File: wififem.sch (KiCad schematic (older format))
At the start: 46 parts, among them J1 Conn_Coaxial, J2 Conn_Coaxial, J3 Conn_Coaxial, J4 Conn_01x05, U1 MCP6566, U2 74HCT04, U3 SE2611T, U4 AP1117-15

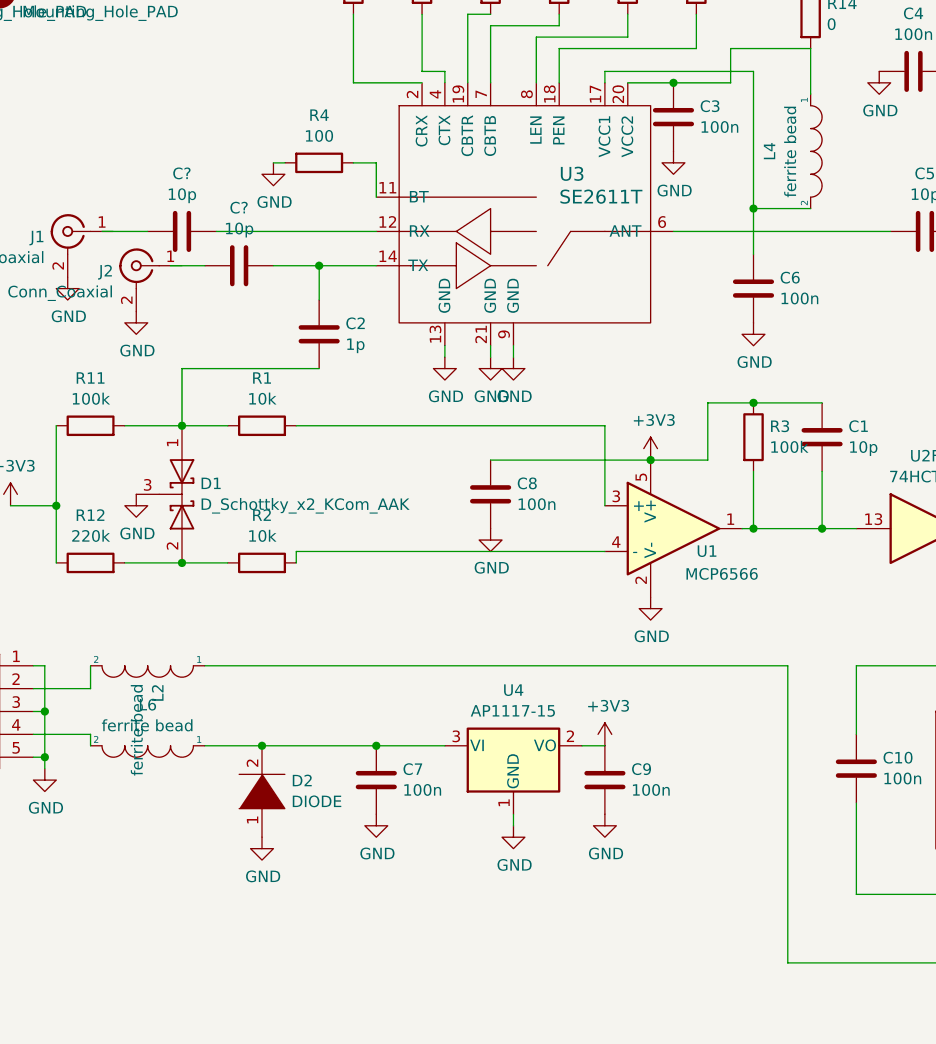
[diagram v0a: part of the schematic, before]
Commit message: Add 2.2u decoupling, some layout changes
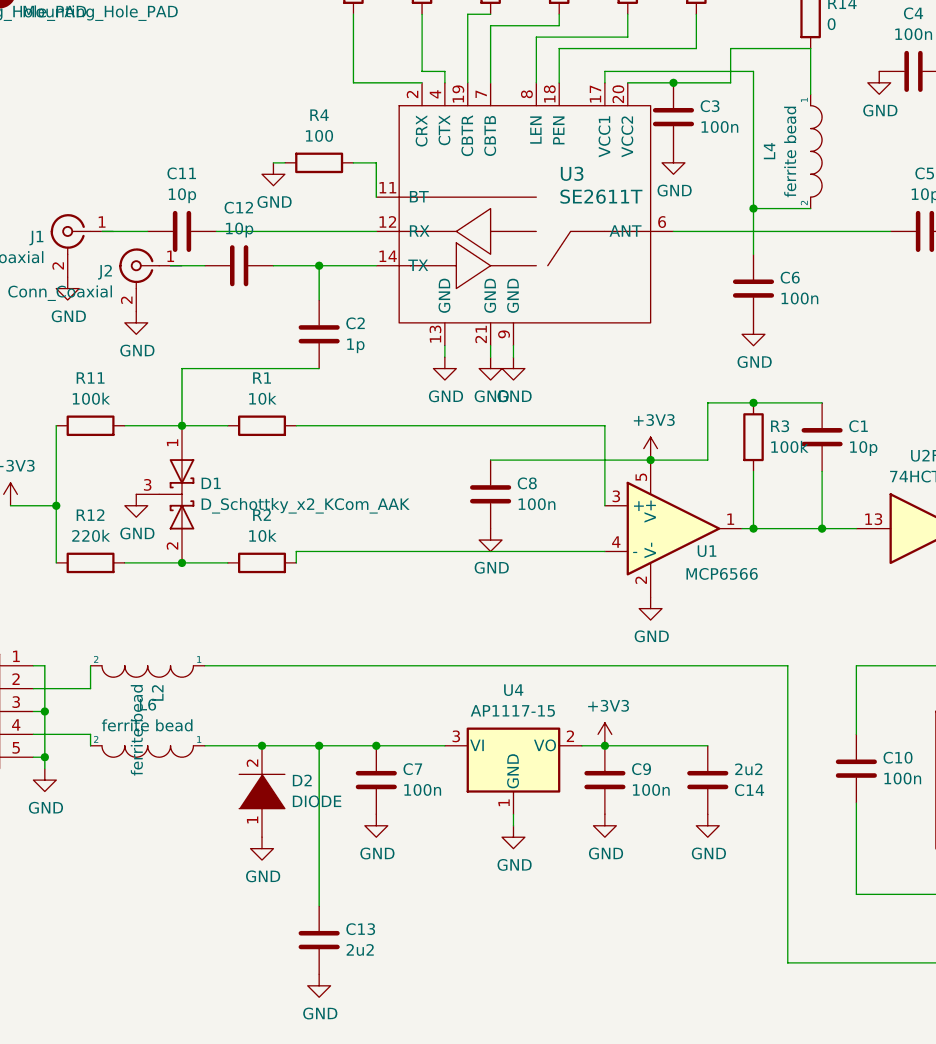
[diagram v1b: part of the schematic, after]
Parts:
- added C13, C14: 2u2, Capacitors_SMD:C_0603_HandSoldering, symbol device:C
- gave numbers to parts that had none: 2
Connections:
- net +3V3: now also C14.1
- net GND: now also C13.1, C14.2
- net at C7.2, D2.2 (A), L6.1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: now also C13.2
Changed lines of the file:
@@
 Connection ~ 3600 3850
 Wire Wire Line
-	6000 4900 5900 4900
+	5900 4900 6450 4900
 Wire Wire Line
 	5600 5250 5600 5200
@@
 Connection ~ 6650 2550
 $Comp
-L device:C C?
+L device:C C11
 U 1 1 5A1C7E8A
 P 4150 2650
-F 0 "C?" V 3898 2650 50  0000 C CNN
+F 0 "C11" V 3898 2650 50  0000 C CNN
 F 1 "10p" V 3989 2650 50  0000 C CNN
 F 2 "Capacitors_SMD:C_0805_HandSoldering" H 4188 2500 50  0001 C CNN
@@
 	4150 3250 4150 3500
 $Comp
-L device:C C?
+L device:C C12
 U 1 1 5A1D3989
 P 4400 2800
-F 0 "C?" V 4148 2800 50  0000 C CNN
+F 0 "C12" V 4148 2800 50  0000 C CNN
 F 1 "10p" V 4239 2800 50  0000 C CNN
 F 2 "Capacitors_SMD:C_0805_HandSoldering" H 4438 2650 50  0001 C CNN
@@
 Wire Wire Line
 	4300 2650 5000 2650
+$Comp
+L device:C C13
+U 1 1 5A1F21AD
+P 4750 5750
+F 0 "C13" H 4635 5704 50  0000 R CNN
+F 1 "2u2" H 4635 5795 50  0000 R CNN
+F 2 "Capacitors_SMD:C_0603_HandSoldering" H 4788 5600 50  0001 C CNN
+F 3 "" H 4750 5750 50  0001 C CNN
+	1    4750 5750
+	-1   0    0    1
+$EndComp
+Wire Wire Line
+	4750 5600 4750 4900
+Connection ~ 4750 4900
+$Comp
+L power:GND #PWR017
+U 1 1 5A1F72C9
+P 4750 5900
+F 0 "#PWR017" H 4750 5650 50  0001 C CNN
+F 1 "GND" H 4755 5727 50  0000 C CNN
+F 2 "" H 4750 5900 50  0001 C CNN
+F 3 "" H 4750 5900 50  0001 C CNN
+	1    4750 5900
+	1    0    0    -1
+$EndComp
+$Comp
+L device:C C14
+U 1 1 5A1F733E
+P 6450 5050
+F 0 "C14" H 6335 5004 50  0000 R CNN
+F 1 "2u2" H 6335 5095 50  0000 R CNN
+F 2 "Capacitors_SMD:C_0603_HandSoldering" H 6488 4900 50  0001 C CNN
+F 3 "" H 6450 5050 50  0001 C CNN
+	1    6450 5050
+	-1   0    0    -1
+$EndComp
+Connection ~ 6000 4900
+$Comp
+L power:GND #PWR031
+U 1 1 5A1FC627
+P 6450 5200
+F 0 "#PWR031" H 6450 4950 50  0001 C CNN
+F 1 "GND" H 6455 5027 50  0000 C CNN
+F 2 "" H 6450 5200 50  0001 C CNN
+F 3 "" H 6450 5200 50  0001 C CNN
+	1    6450 5200
+	1    0    0    -1
+$EndComp
 $EndSCHEMATC

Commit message: Fix libraries for KiCad 5.1
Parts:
- C1, C10, C11, C12, C13, C14, C2, C3, C4, C5, C6, C7, C8, C9: symbol device:C -> Device:C
- D1: symbol device:D_Schottky_x2_KCom_AAK -> Device:D_Schottky_x2_KCom_AAK
- J4: symbol Connector:Conn_01x05 -> Connector_Generic:Conn_01x05
- MK1, MK2, MK3, MK4: symbol Mechanical:Mounting_Hole_PAD -> Mechanical:MountingHole_Pad
- R1, R10, R11, R12, R13, R14, R15, R16, R2, R3, R4, R5, R6, R7, R8, R9: symbol device:R -> Device:R
- U1: symbol linear:MCP6566 -> Comparator:MCP6566
- U2: symbol Logic_74xx:74HCT04 -> 74xx:74HCT04
- U4: symbol regul:AP1117-15 -> Regulator_Linear:AP1117-15
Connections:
- net at R13.1, U2.1, U2.5: no longer U2.3
